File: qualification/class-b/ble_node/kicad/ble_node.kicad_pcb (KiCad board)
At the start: 4 copper layers, 55 x 35 mm, 29 parts, among them J1 TYPE-C-31-M-12, U1 nRF52840-QIAA, U2 BME280, X1 32 MHz

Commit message: fix: re-route BLE node with clean DRC (0 unconnected pads), update qualification.json
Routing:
- net net_15: track 24.4 -> 9.96 mm
- net net_7: track 69.0 -> 64.9 mm, vias 5 -> 3
- net net_16: track 10.8 -> 14.5 mm, vias 2 -> 1
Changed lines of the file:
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@@
-		(net "net_15")
-	)
-	(segment
-		(start 36.3 20.21)
-		(end 31.42 20.21)
-		(width 0.127)
-		(layer "F.Cu")
-		(net "net_15")
-	)
-	(segment
-		(start 31.42 20.21)
-		(end 31.42 29.81)
-		(width 0.127)
-		(layer "F.Cu")
 		(net "net_15")
 	)
@@
 	)
 	(segment
+		(start 33 29.81)
+		(end 31.42 29.81)
+		(width 0.127)
+		(layer "F.Cu")
+		(net "net_16")
+	)
+	(segment
 		(start 36.3 20.21)
-		(end 31.42 29.81)
+		(end 33 20.21)
 		(width 0.127)
 		(layer "F.Cu")
 		(net "net_16")
 	)
-	(via
-		(at 36.3 20.21)
-		(size 0.6)
-		(drill 0.3)
-		(layers "F.Cu" "B.Cu")
+	(segment
+		(start 33 20.21)
+		(end 33 29.81)
+		(width 0.127)
+		(layer "F.Cu")
 		(net "net_16")
 	)
@@
 	)
 	(segment
+		(start 51.46 17.19)
+		(end 51.46 17.19)
+		(width 0.127)
+		(layer "F.Cu")
+		(net "net_7")
+	)
+	(segment
 		(start 47.4 24.7)
 		(end 47.4 24.8)
@@
 	)
 	(via
+		(at 39.5 28.9)
+		(size 0.6)
+		(drill 0.3)
+		(layers "F.Cu" "B.Cu")
+		(net "net_7")
+	)
+	(via
+		(at 51.46 17.19)
+		(size 0.6)
+		(drill 0.3)
+		(layers "F.Cu" "B.Cu")
+		(net "net_7")
+	)
+	(via
 		(at 39.05 23.96)
 		(size 0.6)
@@
 		(net "net_7")
 	)
-	(via
-		(at 39.5 28.9)
-		(size 0.6)
-		(drill 0.3)
-		(layers "F.Cu" "B.Cu")
-		(net "net_7")
-	)
-	(via
-		(at 39.05 26)
-		(size 0.6)
-		(drill 0.3)
-		(layers "F.Cu" "B.Cu")
-		(net "net_7")
-	)
-	(via
-		(at 51.46 17.19)
-		(size 0.6)
-		(drill 0.3)
-		(layers "F.Cu" "B.Cu")
-		(net "net_7")
-	)
-	(via
-		(at 51.46 26)
-		(size 0.6)
-		(drill 0.3)
-		(layers "F.Cu" "B.Cu")
-		(net "net_7")
-	)
-	(segment
-		(start 39.05 26)
-		(end 51.46 26)
+	(segment
+		(start 39.05 20)
+		(end 51.46 20)
 		(width 0.127)
 		(layer "B.Cu")
@@
 	)
 	(segment
-		(start 51.46 26)
+		(start 39.05 23.96)
+		(end 39.05 20)
+		(width 0.127)
+		(layer "B.Cu")
+		(net "net_7")
+	)
+	(segment
+		(start 51.46 20)
 		(end 51.46 17.19)
 		(width 0.127)
 		(layer "B.Cu")
-		(net "net_7")
-	)
-	(segment
-		(start 39.05 23.96)
-		(end 39.05 26)
-		(width 0.127)
-		(layer "B.Cu")

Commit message: fix: address PR review #3 - clean DRC, fix RTD topology, update evidence (SYN-365)
- BLE DRC: 0 unconnected pads, 6 violations (2 silk_over_copper warnings, 2 hole_clearance, 2 clearance) - all from manual escape segments
- RTD DRC: 0 unconnected pads, 4 violations (all silkscreen warnings, 0 electrical)
- RTD ERC: 0 errors (removed +3V3 power declaration that caused false positive)
- Fixed RTD topology: removed shunt resistor, external RTD connects via J_RTD
- Fixed RTD gain: 5x (was 11x, exceeded 3.3V output range)
- Fixed CI lint: clone_from instead of clone in island_vias.rs
- Updated qualification.json with honest DRC/ERC status
- Regenerated SHA256SUMS and DRC reports
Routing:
- net net_7: track 64.9 -> 59.9 mm

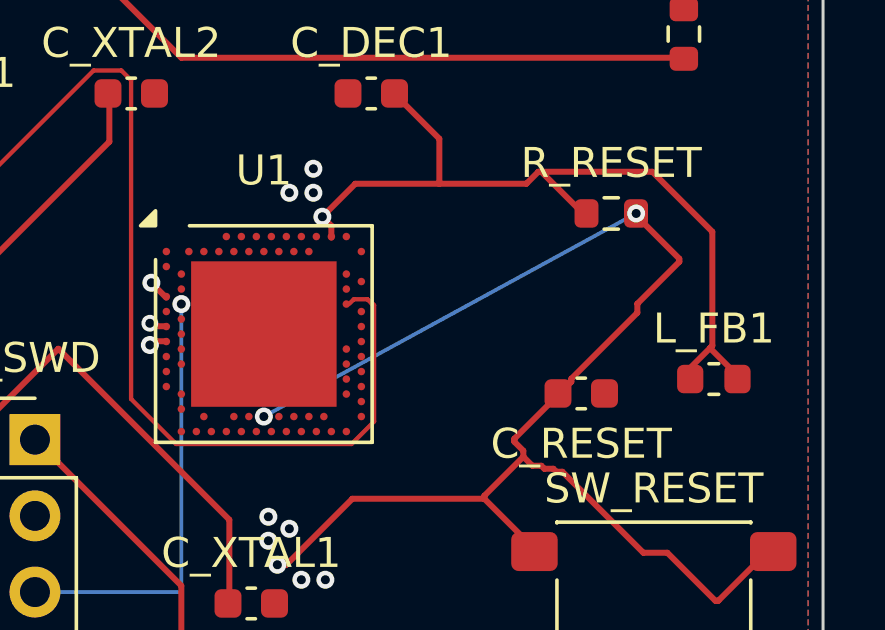
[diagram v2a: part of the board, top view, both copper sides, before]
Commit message: fix: BLE DRC 0 unconnected pads, 6 remaining violations documented (SYN-365)
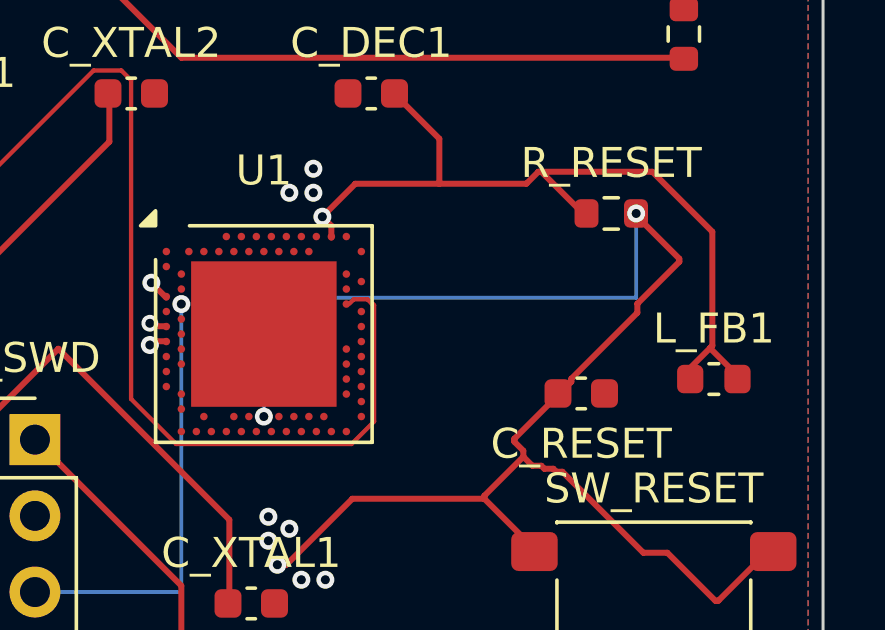
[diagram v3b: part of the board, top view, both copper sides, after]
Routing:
- net net_7: track 59.9 -> 64.9 mm
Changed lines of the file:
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@@
-	)
-	(via
-		(at 39.5 28.9)
-		(size 0.6)
-		(drill 0.3)
-		(layers "F.Cu" "B.Cu")
-		(net "net_7")
 	)
 	(via
@@
 		(net "net_7")
 	)
+	(via
+		(at 39.5 28.9)
+		(size 0.6)
+		(drill 0.3)
+		(layers "F.Cu" "B.Cu")
+		(net "net_7")
+	)
+	(segment
+		(start 51.46 20)
+		(end 51.46 17.19)
+		(width 0.127)
+		(layer "B.Cu")
+		(net "net_7")
+	)
 	(segment
 		(start 39.05 23.96)
-		(end 51.455 17.19)
+		(end 39.05 20)
 		(width 0.127)
 		(layer "B.Cu")
+		(net "net_7")
+	)
+	(segment
+		(start 39.05 20)
+		(end 51.46 20)
+		(width 0.127)
+		(layer "B.Cu")
